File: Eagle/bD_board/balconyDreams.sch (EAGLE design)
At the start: 19 parts, among them IC1 7805L, U1 MKR1000, X2 MKDSN1,5/2-5,08

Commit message: add 2n7001 mosfets for relais outputs
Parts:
- added Q4: 2N7002, transistors_gaui:2N7002
- added R8: (no value), rcl:R-EU_R0805
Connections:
- new net RELAIS_1_OUT: Q4.D, SV1.2
- net GND: now also Q4.S
- net RELAIS_1: now also Q4.G, R8.1; no longer SV1.2
- net VCC: now also R8.2
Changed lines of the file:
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@@
 <?xml version="1.0" encoding="utf-8"?>
 <!DOCTYPE eagle SYSTEM "eagle.dtd">
-<eagle version="7.6.0">
+<eagle version="8.1.0">
 <drawing>
 <settings>
@@
 <setting verticaltext="up"/>
 </settings>
-<grid distance="0.1" unitdist="inch" unit="inch" style="lines" multiple="1" display="yes" altdistance="0.01" altunitdist="inch" altunit="inch"/>
+<grid distance="0.1" unitdist="inch" unit="inch" style="lines" multiple="1" display="no" altdistance="0.01" altunitdist="inch" altunit="inch"/>
 <layers>
 <layer number="1" name="Top" color="4" fill="1" visible="no" active="no"/>
+<layer number="2" name="Route2" color="1" fill="3" visible="no" active="no"/>
+<layer number="3" name="Route3" color="4" fill="3" visible="no" active="no"/>
+<layer number="4" name="Route4" color="1" fill="4" visible="no" active="no"/>
+<layer number="5" name="Route5" color="4" fill="4" visible="no" active="no"/>
+<layer number="6" name="Route6" color="1" fill="8" visible="no" active="no"/>
+<layer number="7" name="Route7" color="4" fill="8" visible="no" active="no"/>
+<layer number="8" name="Route8" color="1" fill="2" visible="no" active="no"/>
+<layer number="9" name="Route9" color="4" fill="2" visible="no" active="no"/>
+<layer number="10" name="Route10" color="1" fill="7" visible="no" active="no"/>
+<layer number="11" name="Route11" color="4" fill="7" visible="no" active="no"/>
+<layer number="12" name="Route12" color="1" fill="5" visible="no" active="no"/>
+<layer number="13" name="Route13" color="4" fill="5" visible="no" active="no"/>
+<layer number="14" name="Route14" color="1" fill="6" visible="no" active="no"/>
+<layer number="15" name="Route15" color="4" fill="6" visible="no" active="no"/>
 <layer number="16" name="Bottom" color="1" fill="1" visible="no" active="no"/>
 <layer number="17" name="Pads" color="2" fill="1" visible="no" active="no"/>
@@
 <layer number="48" name="Document" color="7" fill="1" visible="no" active="no"/>
 <layer number="49" name="Reference" color="7" fill="1" visible="no" active="no"/>
+<layer number="50" name="dxf" color="7" fill="1" visible="no" active="no"/>
 <layer number="51" name="tDocu" color="7" fill="1" visible="no" active="no"/>
 <layer number="52" name="bDocu" color="7" fill="1" visible="no" active="no"/>
@@
 <layer number="97" name="Info" color="7" fill="1" visible="yes" active="yes"/>
 <layer number="98" name="Guide" color="6" fill="1" visible="yes" active="yes"/>
+<layer number="99" name="SpiceOrder" color="5" fill="1" visible="yes" active="yes"/>
+<layer number="250" name="Descript" color="3" fill="1" visible="no" active="no"/>
+<layer number="251" name="SMDround" color="12" fill="11" visible="no" active="no"/>
 </layers>
 <schematic xreflabel="%F%N/%S.%C%R" xrefpart="/%S.%C%R">
@@
 <part name="X1" library="con-phoenix-254" deviceset="MPT2" device=""/>
 <part name="GND12" library="supply1" deviceset="GND" device=""/>
+<part name="Q4" library="transistors_gaui" deviceset="2N7002" device=""/>
+<part name="GND13" library="supply1" deviceset="GND" device=""/>
+<part name="R8" library="rcl" deviceset="R-EU_" device="R0805"/>
+<part name="P+5" library="supply1" deviceset="VCC" device=""/>
 </parts>
 <sheets>
@@
 <instance part="X1" gate="-2" x="20.32" y="71.12"/>
 <instance part="GND12" gate="1" x="15.24" y="66.04"/>
+<instance part="Q4" gate="G$1" x="144.78" y="137.16" rot="MR0"/>
+<instance part="GND13" gate="1" x="137.16" y="129.54"/>
+<instance part="R8" gate="G$1" x="162.56" y="142.24" rot="R90"/>
+<instance part="P+5" gate="VCC" x="162.56" y="152.4"/>
 </instances>
 <busses>
@@
 <wire x1="15.24" y1="71.12" x2="17.78" y2="71.12" width="0.1524" layer="91"/>
 </segment>
+<segment>
+<pinref part="Q4" gate="G$1" pin="S"/>
+<wire x1="139.7" y1="134.62" x2="137.16" y2="134.62" width="0.1524" layer="91"/>
+<wire x1="137.16" y1="134.62" x2="137.16" y2="132.08" width="0.1524" layer="91"/>
+<pinref part="GND13" gate="1" pin="GND"/>
+</segment>
 </net>
 <net name="VCC" class="0">
@@
 <wire x1="200.66" y1="109.22" x2="200.66" y2="111.76" width="0.1524" layer="91"/>
 </segment>
+<segment>
+<pinref part="R8" gate="G$1" pin="2"/>
+<wire x1="162.56" y1="147.32" x2="162.56" y2="149.86" width="0.1524" layer="91"/>
+<pinref part="P+5" gate="VCC" pin="VCC"/>
+</segment>
 </net>
 <net name="RELAIS_7" class="0">
@@
 <net name="RELAIS_1" class="0">
 <segment>
-<pinref part="SV1" gate="1" pin="2"/>
-<wire x1="88.9" y1="139.7" x2="91.44" y2="139.7" width="0.1524" layer="91"/>
-<label x="91.44" y="139.7" size="1.27" layer="95" xref="yes"/>
-</segment>
-<segment>
 <pinref part="U1" gate="G$1" pin="GPIO0"/>
 <wire x1="76.2" y1="83.82" x2="73.66" y2="83.82" width="0.1524" layer="91"/>
 <label x="73.66" y="83.82" size="1.27" layer="95" rot="R180" xref="yes"/>
+</segment>
+<segment>
+<pinref part="Q4" gate="G$1" pin="G"/>
+<pinref part="R8" gate="G$1" pin="1"/>
+<wire x1="149.86" y1="134.62" x2="162.56" y2="134.62" width="0.1524" layer="91"/>
+<wire x1="162.56" y1="134.62" x2="162.56" y2="137.16" width="0.1524" layer="91"/>
+<wire x1="162.56" y1="134.62" x2="165.1" y2="134.62" width="0.1524" layer="91"/>
+<junction x="162.56" y="134.62"/>
+<label x="165.1" y="134.62" size="1.27" layer="95" xref="yes"/>
 </segment>
 </net>
@@
 </segment>
 </net>
+<net name="RELAIS_1_OUT" class="0">
+<segment>
+<pinref part="Q4" gate="G$1" pin="D"/>
+<wire x1="139.7" y1="139.7" x2="137.16" y2="139.7" width="0.1524" layer="91"/>
+<label x="137.16" y="139.7" size="1.27" layer="95" rot="R180" xref="yes"/>
+</segment>
+<segment>
+<pinref part="SV1" gate="1" pin="2"/>
+<wire x1="88.9" y1="139.7" x2="91.44" y2="139.7" width="0.1524" layer="91"/>
+<label x="91.44" y="139.7" size="1.27" layer="95" xref="yes"/>
+</segment>
+</net>

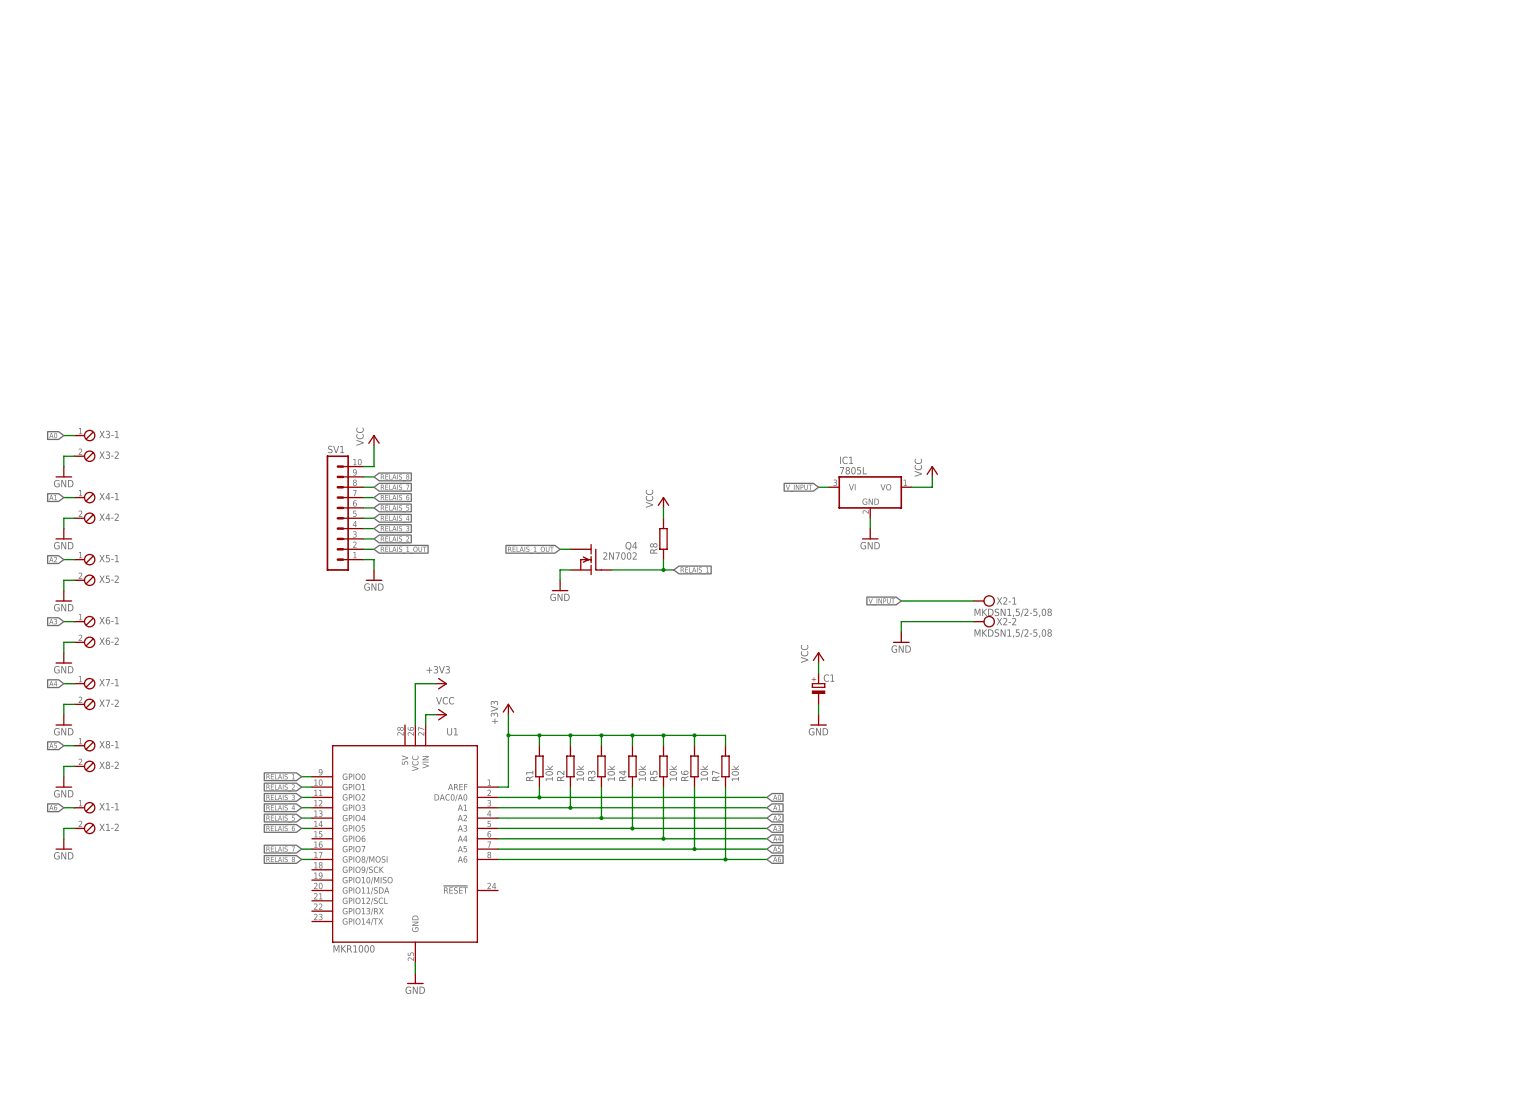
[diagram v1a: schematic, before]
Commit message: add mosfets for all relais outputs
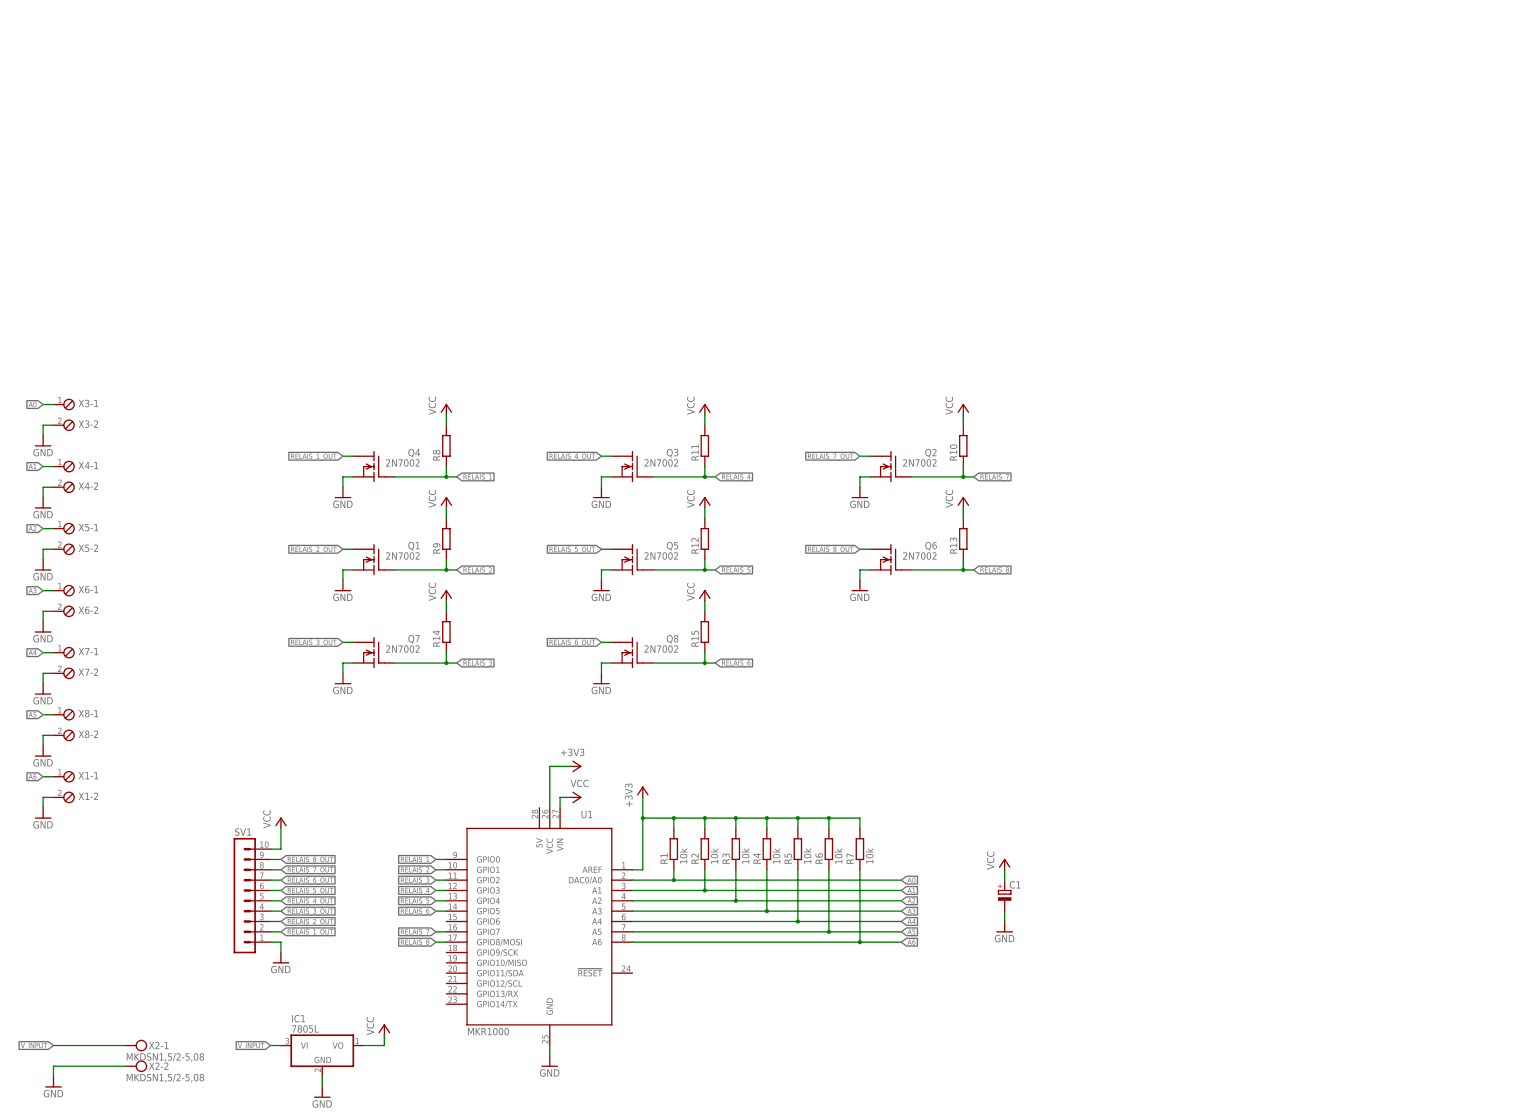
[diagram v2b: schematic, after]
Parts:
- added Q1, Q2, Q3, Q5, Q6, Q7, Q8: 2N7002, transistors_gaui:2N7002
- added R10, R11, R12, R13, R14, R15, R9: (no value), rcl:R-EU_R0805
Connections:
- new net RELAIS_2_OUT: Q1.D, SV1.3
- new net RELAIS_3_OUT: Q7.D, SV1.4
- new net RELAIS_4_OUT: Q3.D, SV1.5
- new net RELAIS_5_OUT: Q5.D, SV1.6
- new net RELAIS_6_OUT: Q8.D, SV1.7
- new net RELAIS_7_OUT: Q2.D, SV1.8
- new net RELAIS_8_OUT: Q6.D, SV1.9
- net GND: now also Q1.S, Q2.S, Q3.S, Q5.S, Q6.S, Q7.S, Q8.S
- net RELAIS_2: now also Q1.G, R9.1; no longer SV1.3
- net RELAIS_3: now also Q7.G, R14.1; no longer SV1.4
- net RELAIS_4: now also Q3.G, R11.1; no longer SV1.5
- net RELAIS_5: now also Q5.G, R12.1; no longer SV1.6
- net RELAIS_6: now also Q8.G, R15.1; no longer SV1.7
- net RELAIS_7: now also Q2.G, R10.1; no longer SV1.8
- net RELAIS_8: now also Q6.G, R13.1; no longer SV1.9
- net VCC: now also R10.2, R11.2, R12.2, R13.2, R14.2, R15.2, R9.2
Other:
- moved on the sheet: C1, IC1, Q4, R1, R2, R3, R4, R5, R6, R7, R8, SV1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

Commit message: wired resistors replaced by SMD
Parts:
- R1, R2, R3, R4, R5, R6, R7: device rcl:R-EU_0309/V -> rcl:R-EU_R0805
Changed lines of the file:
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@@
 <grid distance="0.1" unitdist="inch" unit="inch" style="lines" multiple="1" display="no" altdistance="0.01" altunitdist="inch" altunit="inch"/>
 <layers>
-<layer number="1" name="Top" color="4" fill="1" visible="no" active="no"/>
-<layer number="2" name="Route2" color="1" fill="3" visible="no" active="no"/>
-<layer number="3" name="Route3" color="4" fill="3" visible="no" active="no"/>
-<layer number="4" name="Route4" color="1" fill="4" visible="no" active="no"/>
-<layer number="5" name="Route5" color="4" fill="4" visible="no" active="no"/>
-<layer number="6" name="Route6" color="1" fill="8" visible="no" active="no"/>
-<layer number="7" name="Route7" color="4" fill="8" visible="no" active="no"/>
-<layer number="8" name="Route8" color="1" fill="2" visible="no" active="no"/>
-<layer number="9" name="Route9" color="4" fill="2" visible="no" active="no"/>
-<layer number="10" name="Route10" color="1" fill="7" visible="no" active="no"/>
-<layer number="11" name="Route11" color="4" fill="7" visible="no" active="no"/>
-<layer number="12" name="Route12" color="1" fill="5" visible="no" active="no"/>
-<layer number="13" name="Route13" color="4" fill="5" visible="no" active="no"/>
-<layer number="14" name="Route14" color="1" fill="6" visible="no" active="no"/>
-<layer number="15" name="Route15" color="4" fill="6" visible="no" active="no"/>
-<layer number="16" name="Bottom" color="1" fill="1" visible="no" active="no"/>
-<layer number="17" name="Pads" color="2" fill="1" visible="no" active="no"/>
-<layer number="18" name="Vias" color="2" fill="1" visible="no" active="no"/>
-<layer number="19" name="Unrouted" color="6" fill="1" visible="no" active="no"/>
-<layer number="20" name="Dimension" color="15" fill="1" visible="no" active="no"/>
-<layer number="21" name="tPlace" color="7" fill="1" visible="no" active="no"/>
-<layer number="22" name="bPlace" color="7" fill="1" visible="no" active="no"/>
-<layer number="23" name="tOrigins" color="15" fill="1" visible="no" active="no"/>
-<layer number="24" name="bOrigins" color="15" fill="1" visible="no" active="no"/>
-<layer number="25" name="tNames" color="7" fill="1" visible="no" active="no"/>
-<layer number="26" name="bNames" color="7" fill="1" visible="no" active="no"/>
-<layer number="27" name="tValues" color="7" fill="1" visible="no" active="no"/>
-<layer number="28" name="bValues" color="7" fill="1" visible="no" active="no"/>
+<layer number="1" name="Top" color="4" fill="1" visible="yes" active="no"/>
+<layer number="2" name="Route2" color="1" fill="3" visible="yes" active="no"/>
+<layer number="3" name="Route3" color="4" fill="3" visible="yes" active="no"/>
+<layer number="4" name="Route4" color="1" fill="4" visible="yes" active="no"/>
+<layer number="5" name="Route5" color="4" fill="4" visible="yes" active="no"/>
+<layer number="6" name="Route6" color="1" fill="8" visible="yes" active="no"/>
+<layer number="7" name="Route7" color="4" fill="8" visible="yes" active="no"/>
+<layer number="8" name="Route8" color="1" fill="2" visible="yes" active="no"/>
+<layer number="9" name="Route9" color="4" fill="2" visible="yes" active="no"/>
+<layer number="10" name="Route10" color="1" fill="7" visible="yes" active="no"/>
+<layer number="11" name="Route11" color="4" fill="7" visible="yes" active="no"/>
+<layer number="12" name="Route12" color="1" fill="5" visible="yes" active="no"/>
+<layer number="13" name="Route13" color="4" fill="5" visible="yes" active="no"/>
+<layer number="14" name="Route14" color="1" fill="6" visible="yes" active="no"/>
+<layer number="15" name="Route15" color="4" fill="6" visible="yes" active="no"/>
+<layer number="16" name="Bottom" color="1" fill="1" visible="yes" active="no"/>
+<layer number="17" name="Pads" color="2" fill="1" visible="yes" active="no"/>
+<layer number="18" name="Vias" color="2" fill="1" visible="yes" active="no"/>
+<layer number="19" name="Unrouted" color="6" fill="1" visible="yes" active="no"/>
+<layer number="20" name="Dimension" color="15" fill="1" visible="yes" active="no"/>
+<layer number="21" name="tPlace" color="7" fill="1" visible="yes" active="no"/>
+<layer number="22" name="bPlace" color="7" fill="1" visible="yes" active="no"/>
+<layer number="23" name="tOrigins" color="15" fill="1" visible="yes" active="no"/>
+<layer number="24" name="bOrigins" color="15" fill="1" visible="yes" active="no"/>
+<layer number="25" name="tNames" color="7" fill="1" visible="yes" active="no"/>
+<layer number="26" name="bNames" color="7" fill="1" visible="yes" active="no"/>
+<layer number="27" name="tValues" color="7" fill="1" visible="yes" active="no"/>
+<layer number="28" name="bValues" color="7" fill="1" visible="yes" active="no"/>
 <layer number="29" name="tStop" color="7" fill="3" visible="no" active="no"/>
 <layer number="30" name="bStop" color="7" fill="6" visible="no" active="no"/>
@@
 <layer number="35" name="tGlue" color="7" fill="4" visible="no" active="no"/>
 <layer number="36" name="bGlue" color="7" fill="5" visible="no" active="no"/>
-<layer number="37" name="tTest" color="7" fill="1" visible="no" active="no"/>
-<layer number="38" name="bTest" color="7" fill="1" visible="no" active="no"/>
+<layer number="37" name="tTest" color="7" fill="1" visible="yes" active="no"/>
+<layer number="38" name="bTest" color="7" fill="1" visible="yes" active="no"/>
 <layer number="39" name="tKeepout" color="4" fill="11" visible="no" active="no"/>
 <layer number="40" name="bKeepout" color="1" fill="11" visible="no" active="no"/>
@@
 <layer number="44" name="Drills" color="7" fill="1" visible="no" active="no"/>
 <layer number="45" name="Holes" color="7" fill="1" visible="no" active="no"/>
-<layer number="46" name="Milling" color="3" fill="1" visible="no" active="no"/>
-<layer number="47" name="Measures" color="7" fill="1" visible="no" active="no"/>
-<layer number="48" name="Document" color="7" fill="1" visible="no" active="no"/>
-<layer number="49" name="Reference" color="7" fill="1" visible="no" active="no"/>
-<layer number="50" name="dxf" color="7" fill="1" visible="no" active="no"/>
-<layer number="51" name="tDocu" color="7" fill="1" visible="no" active="no"/>
-<layer number="52" name="bDocu" color="7" fill="1" visible="no" active="no"/>
+<layer number="46" name="Milling" color="3" fill="1" visible="yes" active="no"/>
+<layer number="47" name="Measures" color="7" fill="1" visible="yes" active="no"/>
+<layer number="48" name="Document" color="7" fill="1" visible="yes" active="no"/>
+<layer number="49" name="Reference" color="7" fill="1" visible="yes" active="no"/>
+<layer number="50" name="dxf" color="7" fill="1" visible="yes" active="no"/>
+<layer number="51" name="tDocu" color="7" fill="1" visible="yes" active="no"/>
+<layer number="52" name="bDocu" color="7" fill="1" visible="yes" active="no"/>
 <layer number="90" name="Modules" color="5" fill="1" visible="yes" active="yes"/>
 <layer number="91" name="Nets" color="2" fill="1" visible="yes" active="yes"/>
@@
 <part name="+3V1" library="supply1" deviceset="+3V3" device=""/>
 <part name="+3V2" library="supply1" deviceset="+3V3" device=""/>
-<part name="R1" library="rcl" deviceset="R-EU_" device="0309/V" value="10k"/>
-<part name="R2" library="rcl" deviceset="R-EU_" device="0309/V" value="10k"/>
-<part name="R3" library="rcl" deviceset="R-EU_" device="0309/V" value="10k"/>
-<part name="R4" library="rcl" deviceset="R-EU_" device="0309/V" value="10k"/>
-<part name="R5" library="rcl" deviceset="R-EU_" device="0309/V" value="10k"/>
-<part name="R6" library="rcl" deviceset="R-EU_" device="0309/V" value="10k"/>
-<part name="R7" library="rcl" deviceset="R-EU_" device="0309/V" value="10k"/>
+<part name="R1" library="rcl" deviceset="R-EU_" device="R0805" value="10k"/>
+<part name="R2" library="rcl" deviceset="R-EU_" device="R0805" value="10k"/>
+<part name="R3" library="rcl" deviceset="R-EU_" device="R0805" value="10k"/>
+<part name="R4" library="rcl" deviceset="R-EU_" device="R0805" value="10k"/>
+<part name="R5" library="rcl" deviceset="R-EU_" device="R0805" value="10k"/>
+<part name="R6" library="rcl" deviceset="R-EU_" device="R0805" value="10k"/>
+<part name="R7" library="rcl" deviceset="R-EU_" device="R0805" value="10k"/>
 <part name="X2" library="con-phoenix-508" deviceset="MKDSN1,5/2-5,08" device=""/>
 <part name="X3" library="con-phoenix-254" deviceset="MPT2" device=""/>
